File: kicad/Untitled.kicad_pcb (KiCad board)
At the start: 2 copper layers, 137.3 x 113.5 mm, 36 parts

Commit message: Adding fixed pcb & gerbers
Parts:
- moved REF** 0.29 mm to (128.5, -46.2)
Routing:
- net P4: track 150.3 -> 147.4 mm
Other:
- board size 137.3 x 113.5 mm -> 137.5 x 113.5 mm

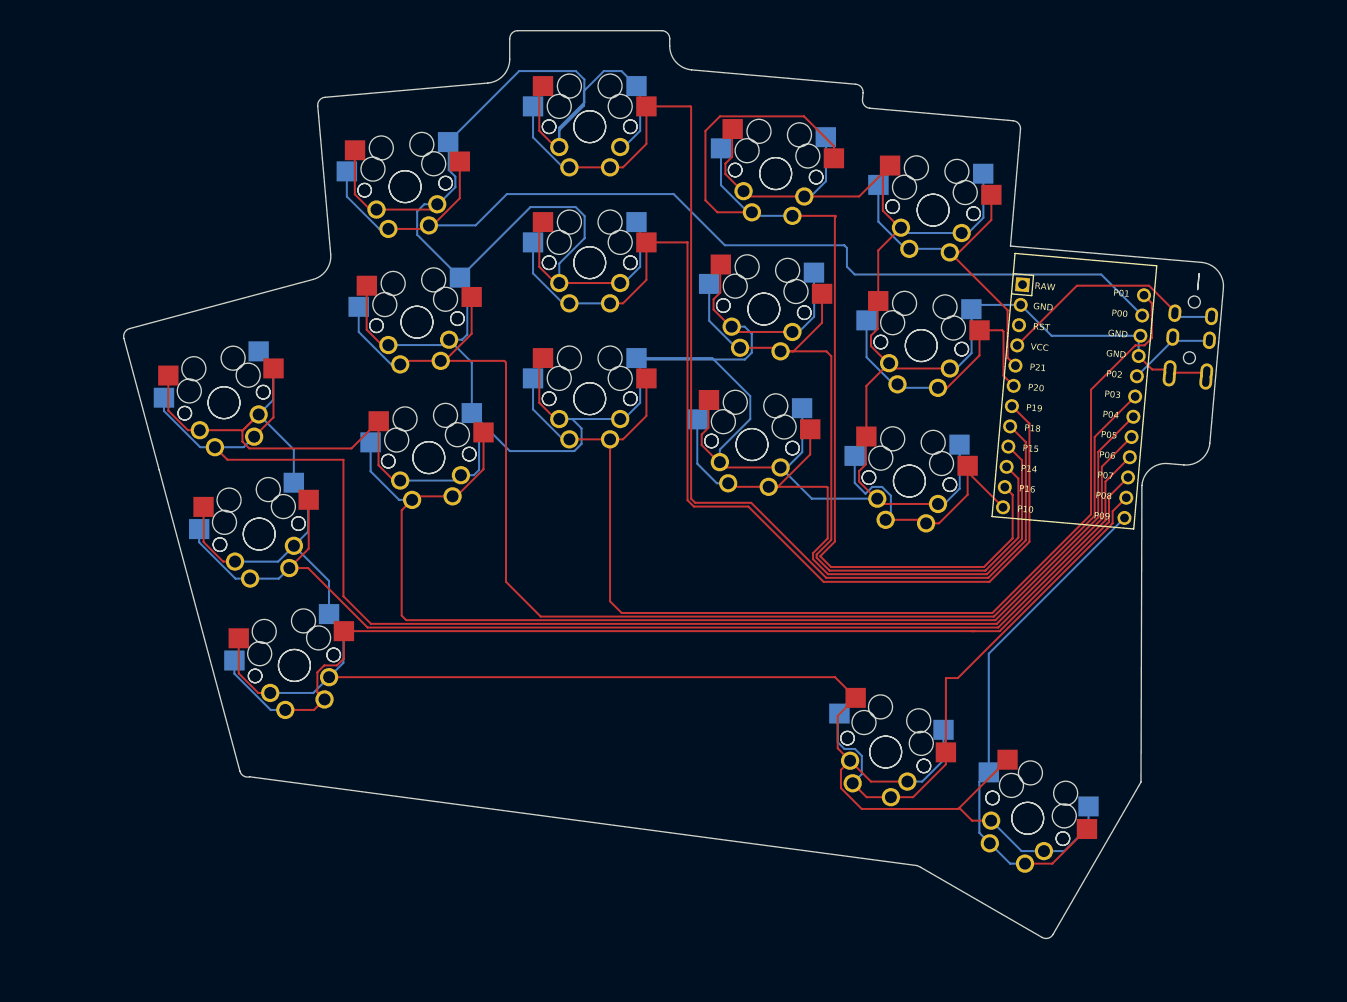
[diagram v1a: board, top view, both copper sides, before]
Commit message: Manually fix pad order, add fill zone for GND
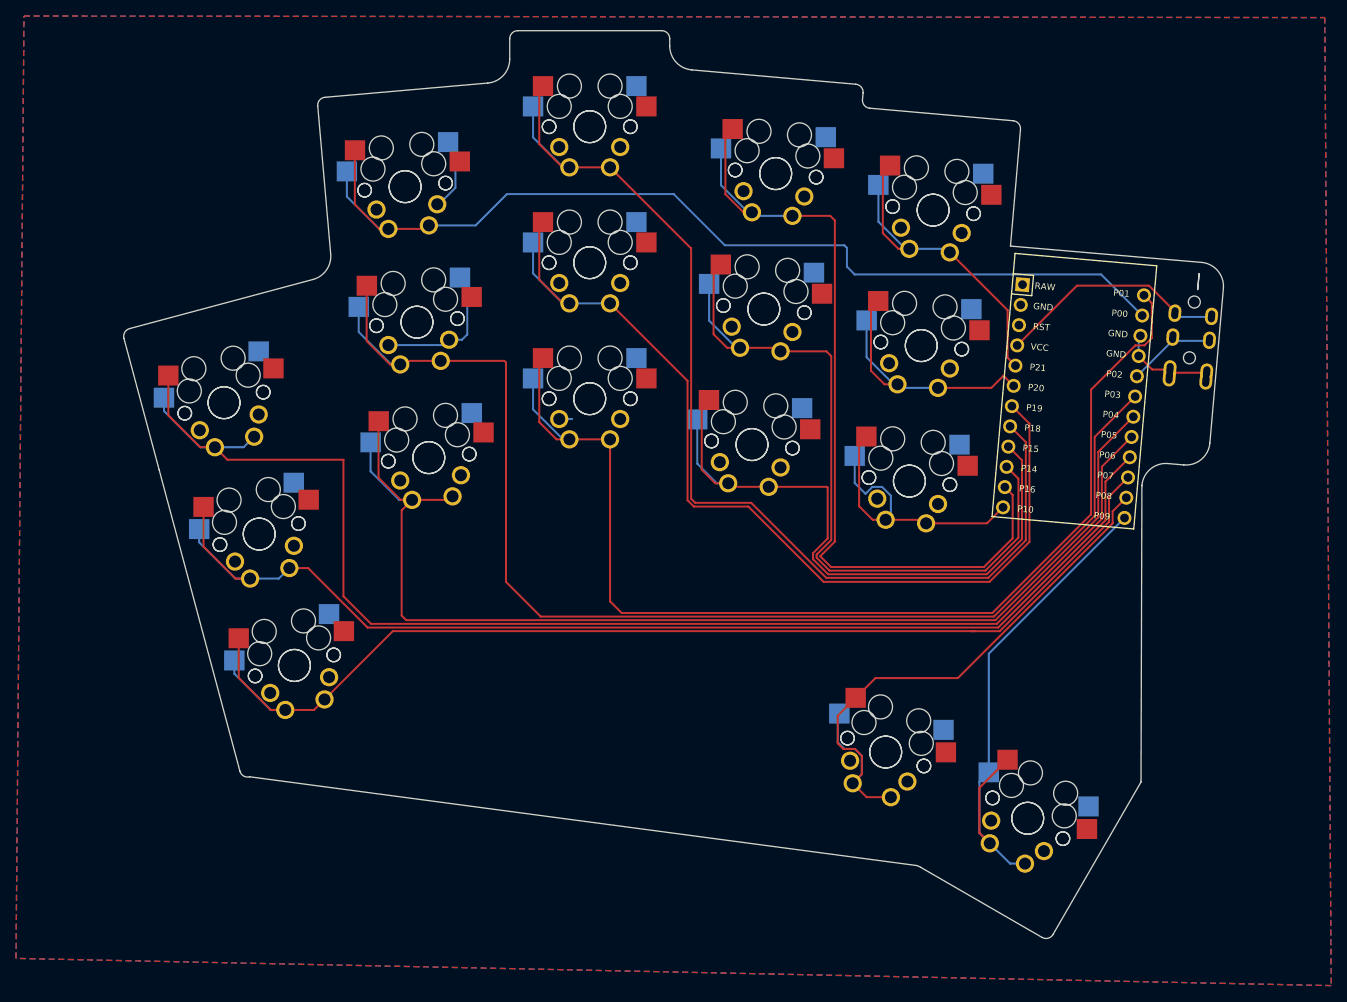
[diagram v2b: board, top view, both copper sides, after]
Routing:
- net GND: track 825.0 -> 37.0 mm
- net P16: track 131.7 -> 106.7 mm
- net P18: track 143.0 -> 133.7 mm
- net P19: track 129.8 -> 120.7 mm
- net P7: track 134.8 -> 141.9 mm
- net P8: track 68.9 -> 75.7 mm
- net P10: track 35.1 -> 38.5 mm
- net P9: track 63.7 -> 66.6 mm
- net P5: track 172.1 -> 175.0 mm
- net P6: track 144.7 -> 147.6 mm
- net P4: track 147.4 -> 149.3 mm
- net P3: track 158.4 -> 160.2 mm
- net P0: track 123.6 -> 125.3 mm
- net P15: track 83.8 -> 85.0 mm
- net P1: track 143.2 -> 144.1 mm
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- added copper zone on B.Cu, net GND
- added copper zone on F.Cu, net GND
